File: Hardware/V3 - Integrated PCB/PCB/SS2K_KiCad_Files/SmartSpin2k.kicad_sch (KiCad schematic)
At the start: 81 parts, among them J1 B4B-XH-AMLFSN, J2 B4B-XH-AMLFSN, J3 B8B-XH-A_LFSN, J4 10118194-0001LF, Q1 S8050, Q2 S8050, SW1 SW_Push, SW2 SW_Push, U1 ESP32-WROOM-32D, U2 TMC2209-LA-T, U3 MAX3232, U4 TPS5430DDA, U5 INTERFACE-CP2102-GMR(QFN28), U6 LM1117-3.3

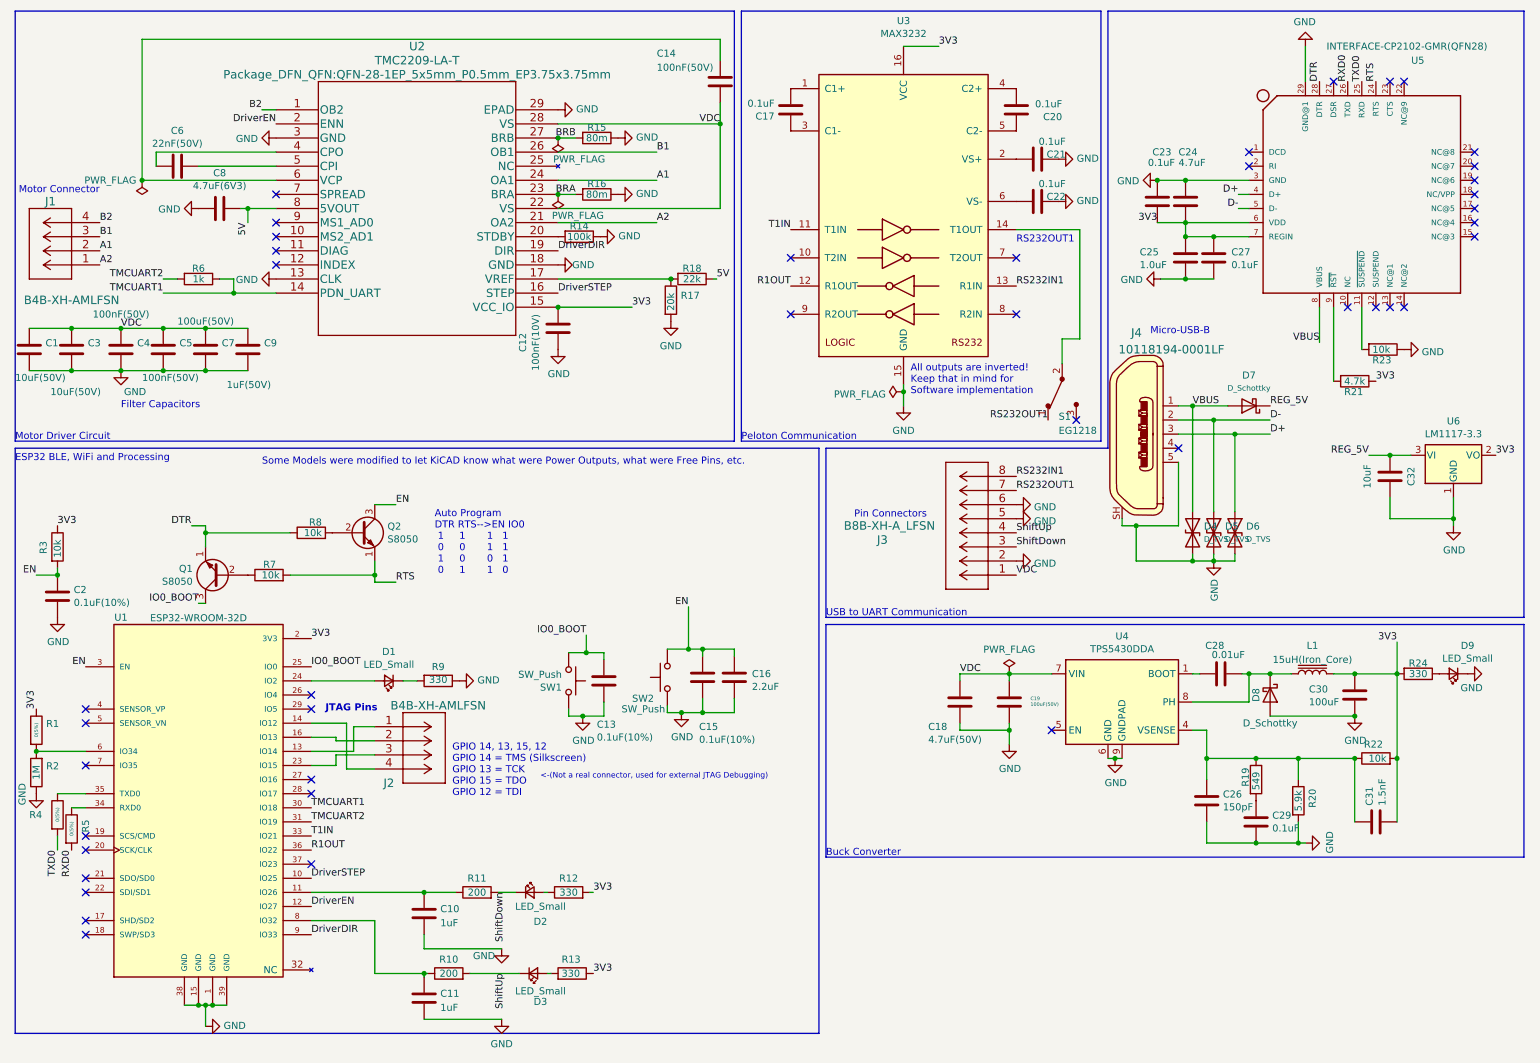
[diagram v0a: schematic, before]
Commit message: New Board Changes to Switch and Edges
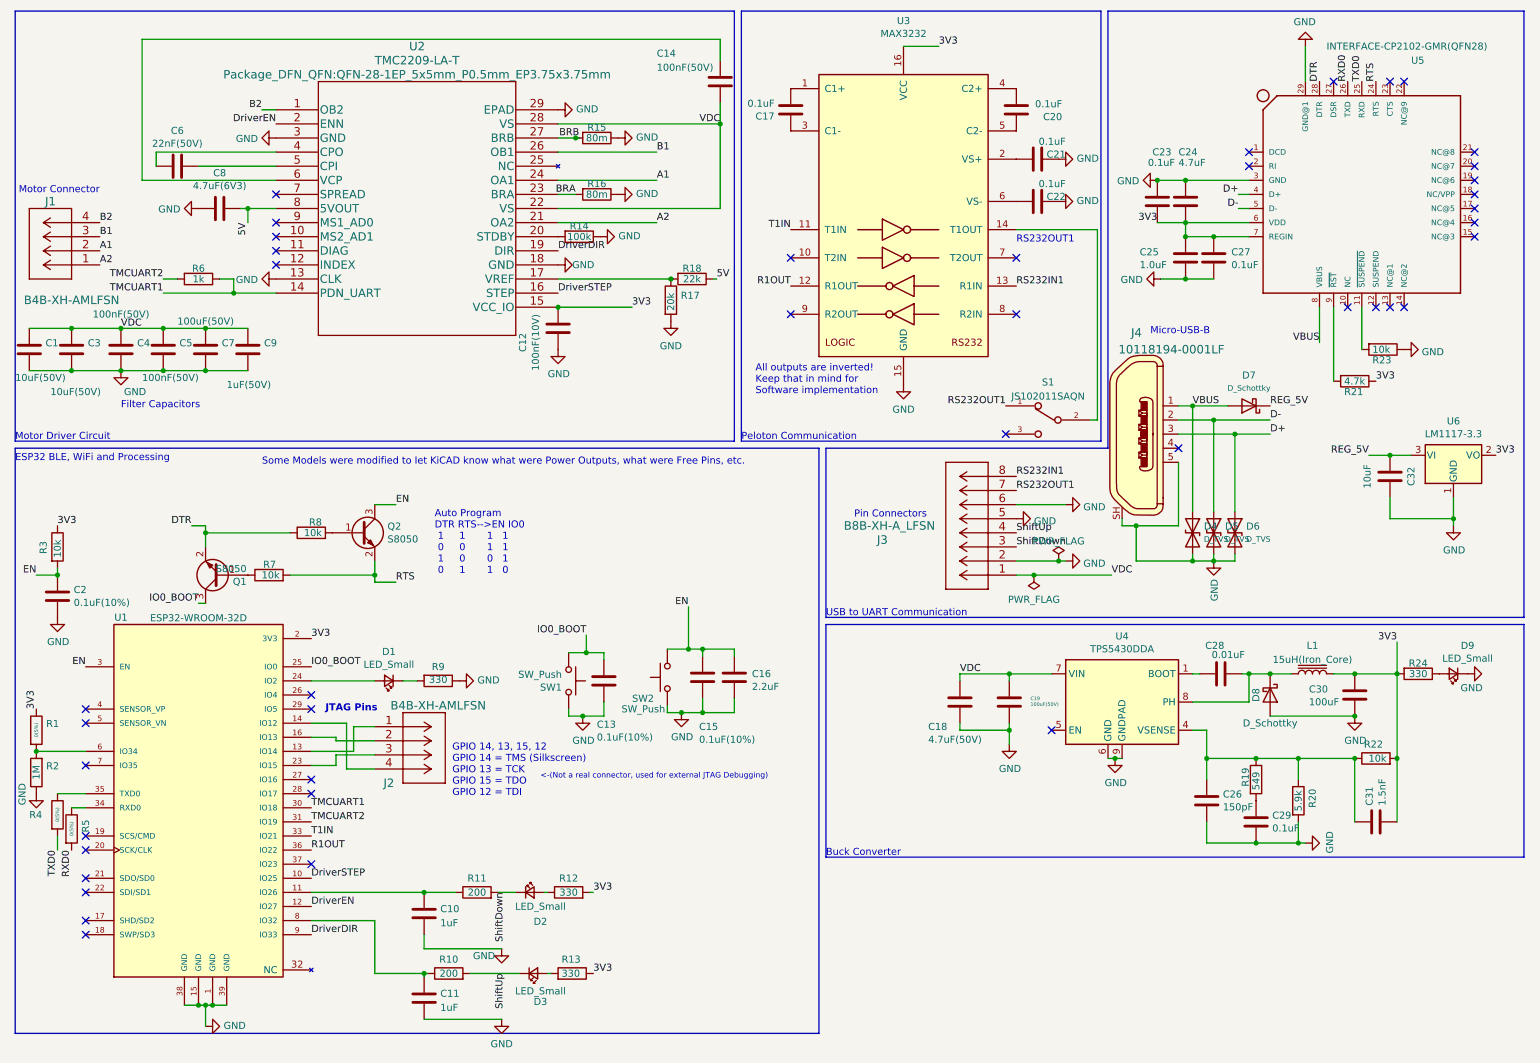
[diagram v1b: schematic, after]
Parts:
- removed S1: EG1218, Button_Switch_SMD:SW_SPDT_PCM12, symbol dk_Slide-Switches:EG1218
- added S1: JS102011SAQN, SW_JS102011SAQN, symbol JS102011SAQN:JS102011SAQN
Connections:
- net DTR: now also Q1.2 (E); no longer Q1.1 (E)
- net RS232OUT1: now also S1.1
- net RTS: now also Q2.2 (E); no longer Q2.1 (E)
- net at R7.1: now also Q1.1 (B); no longer Q1.2 (B)
- net at R8.2: now also Q2.1 (B); no longer Q2.2 (B)
- net at U3.14 (T1OUT): now also S1.2
